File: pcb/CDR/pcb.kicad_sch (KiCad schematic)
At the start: 47 parts, among them J1 Conn_01x03_Male, J2 Conn_01x03_Male, J3 Conn_01x03_Male, J4 Conn_01x03_Male, J5 Conn_01x04_Female, J6 Conn_01x08_Female, J7 Conn_01x02_Female, U1 ATmega328-P, Y1 16MHz

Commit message: cdr pcb
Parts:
- removed C?: 0.1uF, symbol Device:C
- removed C?: 188uf, symbol Device:C
- removed C?: 47uF, symbol Device:C
- removed C?: 30pf, symbol Device:C
- removed C?, Cr?: C, symbol Device:C
- removed C?: 0.33uf, symbol Device:C
- removed D? (x2): 1N47xxA, Diode_THT:D_DO-41_SOD81_P10.16mm_Horizontal, symbol Diode:1N47xxA
- removed D?: 1N4148, Diode_THT:D_DO-35_SOD27_P7.62mm_Horizontal, symbol Diode:1N4148
- removed D?: D, symbol Device:D
- removed J6: Conn_01x08_Female, Connector_PinSocket_2.54mm:PinSocket_1x08_P2.54mm_Vertical, symbol Connector:Conn_01x08_Female
- removed J?: 8.4V batt out, symbol Connector:Conn_01x02_Female
- removed J?: 9 to 20V in, symbol Connector:Conn_01x02_Female
- removed L?: 7 uH, symbol Device:L
- removed Q? (x2): 2N2219, Package_TO_SOT_THT:TO-39-3, symbol Transistor_BJT:2N2219
- removed Q?: IRF9540N, Package_TO_SOT_THT:TO-220-3_Vertical, symbol Transistor_FET:IRF9540N
- removed R? (x2): 2k, symbol Device:R
- removed R? (x4): 500, symbol Device:R
- removed R?: 0.05, symbol Device:R
- removed R?: 1k, symbol Device:R
- removed R?: 100k, symbol Device:R
- removed R?: 200, symbol Device:R
- removed Rsc?: 0.2 Ohm, symbol Device:R
- removed U?: MC33063AD, Package_SO:SOIC-8_3.9x4.9mm_P1.27mm, symbol Regulator_Switching:MC33063AD
- removed U?: LM101, symbol Amplifier_Operational:LM101
- removed U?: LM301, symbol Amplifier_Operational:LM301
- removed U?: LM3420AM5-8.4, TI_National_Semiconductor-LM3420AM5-8.4-*, symbol eec:LM3420AM5-8.4
- added C10, C11, C12, C8: 10uF, Capacitor_SMD:C_1206_3216Metric, symbol Device:C
- added C6: 22uF, Capacitor_SMD:C_1206_3216Metric, symbol Device:C
- added C7: 220uF, Capacitor_SMD:C_1206_3216Metric, symbol Device:C
- added C9: 1uF, Capacitor_SMD:C_1206_3216Metric, symbol Device:C
- added D1: Red, Diode_SMD:D_1206_3216Metric, symbol Device:LED
- added D2: Green, Diode_SMD:D_1206_3216Metric, symbol Device:LED
- added D3, D5: CMPSH3-40MA, Diode_SMD:D_SMB, symbol Device:D
- added D4: CMPSH1-4, Diode_SMD:D_SMA, symbol Device:D
- added D6: 11DQ06, Diode_SMD:D_SMA, symbol Device:D
- added D7: 1V, Diode_SMD:D_SOD-123, symbol Device:D_Zener
- added J10: V Reg in, Connector_PinHeader_2.54mm:PinHeader_1x02_P2.54mm_Vertical, symbol Connector:Conn_01x02_Female
- added J11, J9: V reg out, Connector_PinHeader_2.54mm:PinHeader_1x02_P2.54mm_Vertical, symbol Connector:Conn_01x02_Female
- added J13: V batt, Connector_PinHeader_2.54mm:PinHeader_1x02_P2.54mm_Vertical, symbol Connector:Conn_01x02_Female
- added J14: V chrg out, Connector_PinHeader_2.54mm:PinHeader_1x02_P2.54mm_Vertical, symbol Connector:Conn_01x02_Female
- added J15: V Low Batt in, Connector_PinHeader_2.54mm:PinHeader_1x02_P2.54mm_Vertical, symbol Connector:Conn_01x02_Female
- added J16: V ref in, Connector_PinHeader_2.54mm:PinHeader_1x02_P2.54mm_Vertical, symbol Connector:Conn_01x02_Female
- added J17: V Batt in, Connector_PinHeader_2.54mm:PinHeader_1x02_P2.54mm_Vertical, symbol Connector:Conn_01x02_Female
- added J18: V Low Batt out, Connector_PinHeader_2.54mm:PinHeader_1x02_P2.54mm_Vertical, symbol Connector:Conn_01x02_Female
- added J6: SD Card Reader, Connector_PinHeader_2.54mm:PinHeader_1x06_P2.54mm_Vertical, symbol Connector:Conn_01x06_Female
- added J8: Cell Module, Connector_PinHeader_2.54mm:PinHeader_1x02_P2.54mm_Vertical, symbol Connector:Conn_01x02_Female
- added L1: 330 uH, Inductor_SMD:L_1206_3216Metric, symbol Device:L
- added L2: 10uH, Inductor_SMD:L_1206_3216Metric, symbol Device:L
- added R1: 1K, Resistor_SMD:R_1206_3216Metric, symbol Device:R
- added R10: 0/160, Resistor_SMD:R_1206_3216Metric, symbol Device:R
- added R2: 3.1k, Resistor_SMD:R_1206_3216Metric, symbol Device:R
- added R3, R4: 5.1k, Resistor_SMD:R_1206_3216Metric, symbol Device:R
- added R5: 0.05, Resistor_SMD:R_1206_3216Metric, symbol Device:R
- added R6: 100k, Resistor_SMD:R_1206_3216Metric, symbol Device:R
- added R7: 220k, Resistor_SMD:R_1206_3216Metric, symbol Device:R
- added R8: 50k, Resistor_SMD:R_1206_3216Metric, symbol Device:R
- added R9: 160, Resistor_SMD:R_1206_3216Metric, symbol Device:R
- added U2: LM2574HVM-12, Package_SO:SOIC-14W_7.5x9mm_P1.27mm, symbol Regulator_Switching:LM2574HVM-12
- added U3: LT3650EMSE-8.4-PBF, footprints:LT3650EMSE-8.4-PBF, symbol 2023-02-16_12-26-50:LT3650EMSE-8.4-PBF
- added U4: LM311, Package_SO:SOIC-8_3.9x4.9mm_P1.27mm, symbol Comparator:LM311
- J12: renamed from J?; value V batt -> V Solar; footprint (none) -> Connector_PinHeader_2.54mm:PinHeader_1x02_P2.54mm_Vertical
- J7: value Conn_01x02_Female -> V sys in
- Y1: footprint Crystal:Crystal_SMD_3225-4Pin_3.2x2.5mm -> Crystal:Crystal_SMD_TXC_7M-4Pin_3.2x2.5mm
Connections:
- net GND: now also C10.2, C11.2, C12.1, C6.2, C7.2, C8.2, D3.2 (A), D6.2 (A), J10.2 (Pin_2), J11.2 (Pin_2), J13.2 (Pin_2), J14.2 (Pin_2), J15.2 (Pin_2), J16.2 (Pin_2), J17.2 (Pin_2), J18.2 (Pin_2), J6.1 (Pin_1), J9.2 (Pin_2), R1.1, R7.1, R8.2, U2.4 (SGND), U2.5 (~{ON}/OFF), U2.6 (PGND), U3.13 (EPAD), U3.6 (TIMER), U3.7 (RNG/SS), U3.8 (NTC), U4.4 (V-)
- net VCC: now also J6.2 (Pin_2)
- net at J12.1 (Pin_1): now also D5.2 (A)
- net at U1.2 (PD0): now also J6.6 (Pin_6)
- net at U1.3 (PD1): now also J6.5 (Pin_5)
- net at U1.4 (PD2): now also J6.4 (Pin_4)
- net at U1.5 (PD3): now also J6.3 (Pin_3)
- net at U1.12 (PD6): now also J8.1 (Pin_1)
- net at U1.13 (PD7): now also J8.2 (Pin_2)
- net at U1.14 (PB0): now also J15.1 (Pin_1)
- net at U1.26 (PC3): now also C12.2, R10.1; no longer J4.3 (Pin_3)
- new net: C8.1, D1.2 (A), D2.2 (A), D5.1 (K), U3.1 (VIN), U3.2 (CLP), U3.3 (*SHDN)
- new net: D1.1 (K), R3.1
- new net: R6.2, R7.2, U4.3 (-)
- new net: D6.1 (K), L1.1, U2.12 (OUT)
- new net: C7.1, J11.1 (Pin_1), J9.1 (Pin_1), L1.2, R2.1
- new net: C11.1, J18.1 (Pin_1), R9.2
- new net: D7.1 (K), U4.7
- new net: D7.2 (A), R8.1, R9.1
- new net: L2.1, R5.1, U3.10 (SENSE)
- new net: C10.1, D4.2 (A), J13.1 (Pin_1), J14.1 (Pin_1), R5.2, U3.9 (BAT)
- new net: R1.2, R2.2, U2.3 (FB)
- new net: R3.2, U3.5 (*FAULT)
- new net: C9.2, D4.1 (K), U3.11 (BOOST)
- new net: J4.3 (Pin_3), R10.2
- new net: D2.1 (K), R4.1
- new net: J16.1 (Pin_1), U4.2 (+)
- new net: J17.1 (Pin_1), R6.1, U4.8 (V+)
- new net: C9.1, D3.1 (K), L2.2, U3.12 (SW)
- new net: R4.2, U3.4 (*CHRG)
- new net: C6.1, J10.1 (Pin_1), U2.10 (VIN)
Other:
- moved on the sheet: C1, C2, C3, C4, C5, J1, J12, J7, U1, Y1

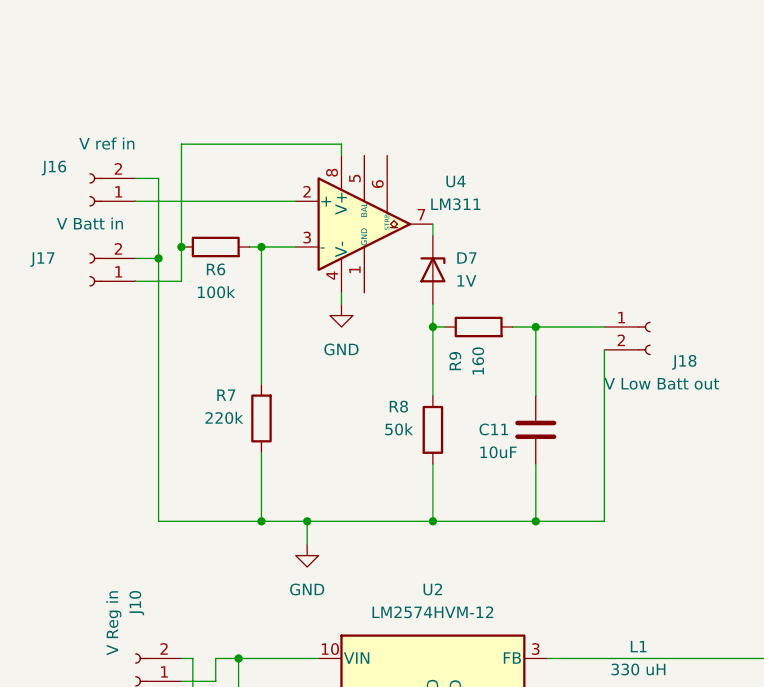
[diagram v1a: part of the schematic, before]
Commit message: decoupling cap on lm 311
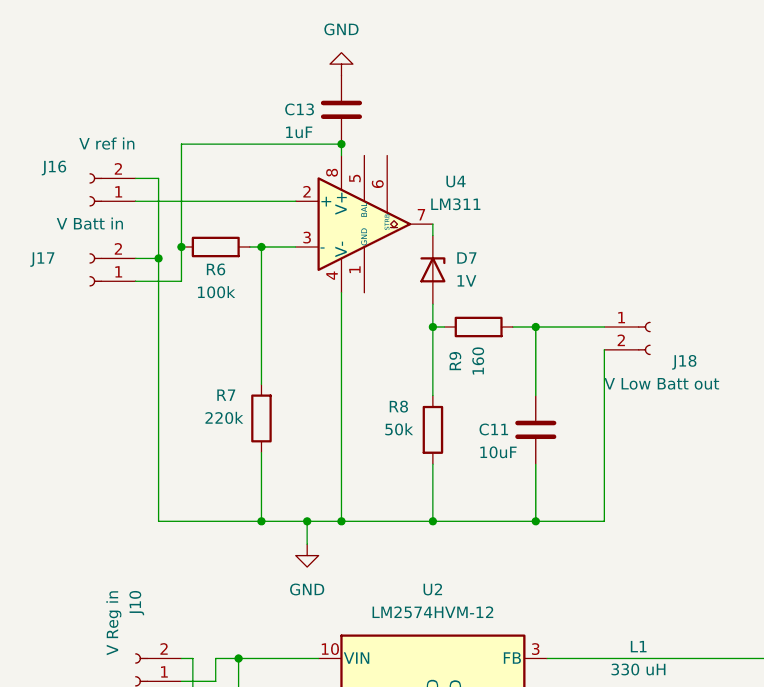
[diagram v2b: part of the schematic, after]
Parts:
- added C13: 1uF, Capacitor_SMD:C_1206_3216Metric, symbol Device:C
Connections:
- net GND: now also C13.1
- net at J17.1 (Pin_1), R6.1, U4.8 (V+): now also C13.2
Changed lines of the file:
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@@
   (junction (at 35.56 83.82) (diameter 0) (color 0 0 0 0)
   )
+  (junction (at 46.99 26.67) (diameter 0) (color 0 0 0 0)
+  )
   (junction (at 237.49 123.19) (diameter 0) (color 0 0 0 0)
   )
@@
   (junction (at 237.49 69.85) (diameter 0) (color 0 0 0 0)
   )
+  (junction (at 46.99 68.58) (diameter 0) (color 0 0 0 0)
+  )
   (junction (at 35.56 104.14) (diameter 0) (color 0 0 0 0)
   )
@@
     (stroke (width 0) (type default) (color 0 0 0 0))
   )
-  (wire (pts (xy 46.99 44.45) (xy 46.99 43.18))
-    (stroke (width 0) (type default) (color 0 0 0 0))
-  )
   (wire (pts (xy 240.03 125.73) (xy 248.92 125.73))
     (stroke (width 0) (type default) (color 0 0 0 0))
@@
     (stroke (width 0) (type default) (color 0 0 0 0))
   )
-  (wire (pts (xy 43.18 68.58) (xy 57.15 68.58))
+  (wire (pts (xy 43.18 68.58) (xy 46.99 68.58))
     (stroke (width 0) (type default) (color 0 0 0 0))
   )
@@
     (stroke (width 0) (type default) (color 0 0 0 0))
   )
+  (wire (pts (xy 46.99 68.58) (xy 57.15 68.58))
+    (stroke (width 0) (type default) (color 0 0 0 0))
+  )
   (wire (pts (xy 162.56 189.23) (xy 163.83 189.23))
     (stroke (width 0) (type default) (color 0 0 0 0))
@@
   )
   (wire (pts (xy 71.12 104.14) (xy 90.17 104.14))
+    (stroke (width 0) (type default) (color 0 0 0 0))
+  )
+  (wire (pts (xy 46.99 43.18) (xy 46.99 68.58))
     (stroke (width 0) (type default) (color 0 0 0 0))
   )
@@
     (pin "2")
   )
+  (symbol (lib_id "power:GND") (at 46.99 19.05 180) (unit 1)
+    (in_bom yes) (on_board yes) (fields_autoplaced)
+    (property "Reference" "#PWR01" (id 0) (at 46.99 12.7 0)
+      (effects (font (size 1.27 1.27)) hide)
+    )
+    (property "Value" "GND" (id 1) (at 46.99 13.97 0))
+    (property "Footprint" "" (id 2) (at 46.99 19.05 0)
+      (effects (font (size 1.27 1.27)) hide)
+    )
+    (property "Datasheet" "" (id 3) (at 46.99 19.05 0)
+      (effects (font (size 1.27 1.27)) hide)
+    )
+    (pin "1")
+  )
   (symbol (lib_id "Device:R") (at 38.1 57.15 180) (unit 1)
     (in_bom yes) (on_board yes)
@@
     (pin "1")
     (pin "2")
-  )
-  (symbol (lib_id "power:GND") (at 46.99 44.45 0) (unit 1)
-    (in_bom yes) (on_board yes) (fields_autoplaced)
-    (property "Reference" "#PWR0109" (id 0) (at 46.99 50.8 0)
-      (effects (font (size 1.27 1.27)) hide)
-    )
-    (property "Value" "GND" (id 1) (at 46.99 49.53 0))
-    (property "Footprint" "" (id 2) (at 46.99 44.45 0)
-      (effects (font (size 1.27 1.27)) hide)
-    )
-    (property "Datasheet" "" (id 3) (at 46.99 44.45 0)
-      (effects (font (size 1.27 1.27)) hide)
-    )
-    (pin "1")
   )
   (symbol (lib_id "power:GND") (at 127 69.85 0) (unit 1)
@@
     )
     (property "Datasheet" "~" (id 3) (at 123.19 93.98 0)
+      (effects (font (size 1.27 1.27)) hide)
+    )
+    (pin "1")
+    (pin "2")
+  )
+  (symbol (lib_id "Device:C") (at 46.99 22.86 0) (unit 1)
+    (in_bom yes) (on_board yes)
+    (property "Reference" "C13" (id 0) (at 40.64 22.86 0)
+      (effects (font (size 1.27 1.27)) (justify left))
+    )
+    (property "Value" "1uF" (id 1) (at 40.64 25.4 0)
+      (effects (font (size 1.27 1.27)) (justify left))
+    )
+    (property "Footprint" "Capacitor_SMD:C_1206_3216Metric" (id 2) (at 47.9552 26.67 0)
+      (effects (font (size 1.27 1.27)) hide)
+    )
+    (property "Datasheet" "~" (id 3) (at 46.99 22.86 0)
       (effects (font (size 1.27 1.27)) hide)
     )
@@
   )
   (symbol_instances
+    (path "/0c4dd976-80b9-41ff-94d0-b216f55bfb5a"
+      (reference "#PWR01") (unit 1) (value "GND") (footprint "")
+    )
     (path "/9de2fc93-a40d-4e62-9ae7-510ab865ad3c"
       (reference "#PWR0101") (unit 1) (value "VCC") (footprint "")
@@
       (reference "#PWR0108") (unit 1) (value "GND") (footprint "")
     )
-    (path "/3536f602-7820-4243-8ece-a4c863868343"
-      (reference "#PWR0109") (unit 1) (value "GND") (footprint "")
-    )
     (path "/2e18c063-041b-4967-aac1-5a9a6a178bfb"
       (reference "#PWR0110") (unit 1) (value "GND") (footprint "")
@@
       (reference "C12") (unit 1) (value "10uF") (footprint "Capacitor_SMD:C_1206_3216Metric")
     )
+    (path "/b8f908f3-5c73-42b6-ae4b-65cbe05e9c22"
+      (reference "C13") (unit 1) (value "1uF") (footprint "Capacitor_SMD:C_1206_3216Metric")
+    )
     (path "/07143691-e57a-475f-bab5-c5ef98cfc401"

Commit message: major updates to interface, analytics and security
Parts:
- added R11: 1k, Resistor_SMD:R_1206_3216Metric, symbol Device:R
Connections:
- net at D7.1 (K), U4.7: now also R11.2
- net at C13.2, J17.1 (Pin_1), R6.1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: now also R11.1
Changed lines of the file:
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@@
   (junction (at 68.58 46.99) (diameter 0) (color 0 0 0 0)
   )
+  (junction (at 57.15 35.56) (diameter 0) (color 0 0 0 0)
+  )
   (junction (at 240.03 109.22) (diameter 0) (color 0 0 0 0)
   )
@@
     (stroke (width 0) (type default) (color 0 0 0 0))
   )
+  (wire (pts (xy 57.15 34.29) (xy 57.15 35.56))
+    (stroke (width 0) (type default) (color 0 0 0 0))
+  )
   (wire (pts (xy 30.48 104.14) (xy 35.56 104.14))
     (stroke (width 0) (type default) (color 0 0 0 0))
@@
   )
   (wire (pts (xy 167.64 104.14) (xy 199.39 104.14))
+    (stroke (width 0) (type default) (color 0 0 0 0))
+  )
+  (wire (pts (xy 46.99 26.67) (xy 57.15 26.67))
     (stroke (width 0) (type default) (color 0 0 0 0))
   )
@@
   )
   (symbol (lib_id "Comparator:LM311") (at 49.53 35.56 0) (unit 1)
-    (in_bom yes) (on_board yes) (fields_autoplaced)
-    (property "Reference" "U4" (id 0) (at 59.69 30.861 0))
-    (property "Value" "LM311" (id 1) (at 59.69 33.401 0))
+    (in_bom yes) (on_board yes)
+    (property "Reference" "U4" (id 0) (at 43.18 41.91 0))
+    (property "Value" "LM311" (id 1) (at 43.18 44.45 0))
     (property "Footprint" "Package_SO:SOIC-8_3.9x4.9mm_P1.27mm" (id 2) (at 49.53 35.56 0)
       (effects (font (size 1.27 1.27)) hide)
@@
     (pin "1")
   )
+  (symbol (lib_id "Device:R") (at 57.15 30.48 0) (unit 1)
+    (in_bom yes) (on_board yes)
+    (property "Reference" "R11" (id 0) (at 60.96 25.4 0))
+    (property "Value" "1k" (id 1) (at 60.96 27.94 0))
+    (property "Footprint" "Resistor_SMD:R_1206_3216Metric" (id 2) (at 55.372 30.48 90)
+      (effects (font (size 1.27 1.27)) hide)
+    )
+    (property "Datasheet" "~" (id 3) (at 57.15 30.48 0)
+      (effects (font (size 1.27 1.27)) hide)
+    )
+    (pin "1")
+    (pin "2")
+  )
   (symbol (lib_id "Regulator_Switching:LM2574HVM-12") (at 57.15 86.36 0) (unit 1)
     (in_bom yes) (on_board yes) (fields_autoplaced)
@@
       (reference "R10") (unit 1) (value "0/160") (footprint "Resistor_SMD:R_1206_3216Metric")
     )
+    (path "/cfaec59e-9bc0-4344-a7f4-2dbc79e9db61"
+      (reference "R11") (unit 1) (value "1k") (footprint "Resistor_SMD:R_1206_3216Metric")
+    )
     (path "/c17a108f-f617-4738-a471-dfbb117640e6"

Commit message: Merge branch 'main' of http://github.com/dgibb/sdp into main
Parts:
- removed J10: V Reg in, Connector_PinHeader_2.54mm:PinHeader_1x02_P2.54mm_Vertical, symbol Connector:Conn_01x02_Female
- removed J11, J9: V reg out, Connector_PinHeader_2.54mm:PinHeader_1x02_P2.54mm_Vertical, symbol Connector:Conn_01x02_Female
- removed J14: V chrg out, Connector_PinHeader_2.54mm:PinHeader_1x02_P2.54mm_Vertical, symbol Connector:Conn_01x02_Female
- removed J15: V Low Batt in, Connector_PinHeader_2.54mm:PinHeader_1x02_P2.54mm_Vertical, symbol Connector:Conn_01x02_Female
- removed J16: V ref in, Connector_PinHeader_2.54mm:PinHeader_1x02_P2.54mm_Vertical, symbol Connector:Conn_01x02_Female
- removed J17: V Batt in, Connector_PinHeader_2.54mm:PinHeader_1x02_P2.54mm_Vertical, symbol Connector:Conn_01x02_Female
- removed J18: V Low Batt out, Connector_PinHeader_2.54mm:PinHeader_1x02_P2.54mm_Vertical, symbol Connector:Conn_01x02_Female
- removed J7: V sys in, Connector_PinHeader_2.54mm:PinHeader_1x02_P2.54mm_Vertical, symbol Connector:Conn_01x02_Female
- removed J8: Cell Module, Connector_PinHeader_2.54mm:PinHeader_1x02_P2.54mm_Vertical, symbol Connector:Conn_01x02_Female
- added C?: 10uF, Capacitor_SMD:C_1206_3216Metric, symbol Device:C
- added J?: cell data headers, symbol Connector:Conn_01x03_Female
- added J?: cell power headers, symbol Connector:Conn_01x03_Female
- added R? (x2): 0, Resistor_SMD:R_1206_3216Metric, symbol Device:R
- added R?: 0/160, Resistor_SMD:R_1206_3216Metric, symbol Device:R
- L1: footprint Inductor_SMD:L_1206_3216Metric -> Inductor_SMD:L_Bourns-SRU8028_8.0x8.0mm
- U4: footprint Package_SO:SOIC-8_3.9x4.9mm_P1.27mm -> Package_DIP:DIP-8_W7.62mm
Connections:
- net GND: now also C10.1, D4.2 (A), J13.1 (Pin_1), R5.2, U3.9 (BAT), C?.1, J?.2 (Pin_2), J?.3 (Pin_3), R?.2
- net VCC: now also C7.1, L1.2, R2.1, J?.1 (Pin_1), R?.2
- net at R6.2, R7.2: now also U4.2 (+); no longer U4.3 (-)
- net at J6.3 (Pin_3): now also U1.18 (PB4), J?.1 (Pin_1); no longer U1.5 (PD3)
- net at J6.4 (Pin_4): now also U1.17 (PB3); no longer U1.4 (PD2)
- net at J6.5 (Pin_5): now also U1.19 (PB5); no longer U1.3 (PD1)
- net at J6.6 (Pin_6): now also U1.6 (PD4); no longer U1.2 (PD0)
- net at C11.1, R9.2: now also U1.15 (PB1)
- net at U1.14 (PB0): now also J?.2 (Pin_2)
- net at C13.2, R11.1, R6.1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: now also C6.1, U2.10 (VIN), R?.1
- net at U1.25 (PC2): now also C?.2, R?.1; no longer J3.3 (Pin_3)
- net at U1.13 (PD7): now also J?.3 (Pin_3)
- net at U1.23 (PC0): no longer J1.3 (Pin_3)
- new net: R?.1, U4.3 (-)
- new net: J3.3 (Pin_3), R?.2
- new net: J1.3 (Pin_3), U1.5 (PD3)
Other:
- moved on the sheet: J12
